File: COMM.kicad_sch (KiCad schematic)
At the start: 14 parts, among them J1 SMA Conn. (RFPC-SMA30-F), SW1 Inhibit Switch (SS5GLD2), U1 XBee Module (XBP9B-DMSTB002)

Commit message: Addressed most comments from McPherson, modified schematic.
Signed-off-by: Logan Tolbert <xem6df@virginia.edu>
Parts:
- removed D2: Voltage Converter DMR (1N4002), Diode_THT:D_DO-41_SOD81_P10.16mm_Horizontal, symbol Diode:1N4002
- added C2: 10 μF, C_10uF:CAPC1005X70N, symbol Device:C
- added D1: GRN_DMR, LED_THT:LED_D5.0mm, symbol Device:LED
- added R3: 140 Ω, R_470O:RESC6332X65N, symbol Device:R_US
- D2: renamed from D1; value LED -> GRN_XB
- D3: value LED -> YLW_ASC_XB
- R1: value 10 kΩ -> 130 Ω; footprint R_10kO:RESC1005X40N -> R_470O:RESC6332X65N
- R2: value 470 Ω -> 130 Ω
- renumbered C2 to C3, C3 to C4, C4 to C5
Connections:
- net +3.3V: now also R2.2
- net Associate/DIO5_XB: now also R3.2; no longer D3.2 (A)
- net GND: now also C2.2, D1.1 (K); no longer R1.1
- net Voltage Converter/VIN: no longer R2.2
- net at SW1.3 (C): no longer R1.2
- net Voltage Step-Up (TPS61085)/VIN: now reaches H1.51
- net Voltage Step-Up (TPS61085)/VIN: now also R1.2, C2.1
- net HST_RXD_DMR: no longer names the net of H2.25
- net HST_TXD_DMR: no longer names the net of H2.27
- new net: D1.2 (A), R1.1
- new net: D3.2 (A), R3.1
- no-connect marks 24 -> 27
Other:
- sheet DMR818S-U 2W RF Module renamed DMR818S 5W RF Module
- sheet Voltage Converter XB renamed Voltage Converter
- added sheet Voltage Step-Up (TPS61085) (TPS61085.kicad_sch)
- sheet DMR818S 5W RF Module ports: added none; removed HST_RXD, HST_TXD
- note added: "5V Power Supply From EPS for XBee Module"
- note added: "D3-LED ON indicates XBee is enabled."
- note removed: "5V Power Supply From EPS"
- moved on the sheet: C1, C3, C4, C5, D2, D3, H1, H2, J1, R2, SW1, U1

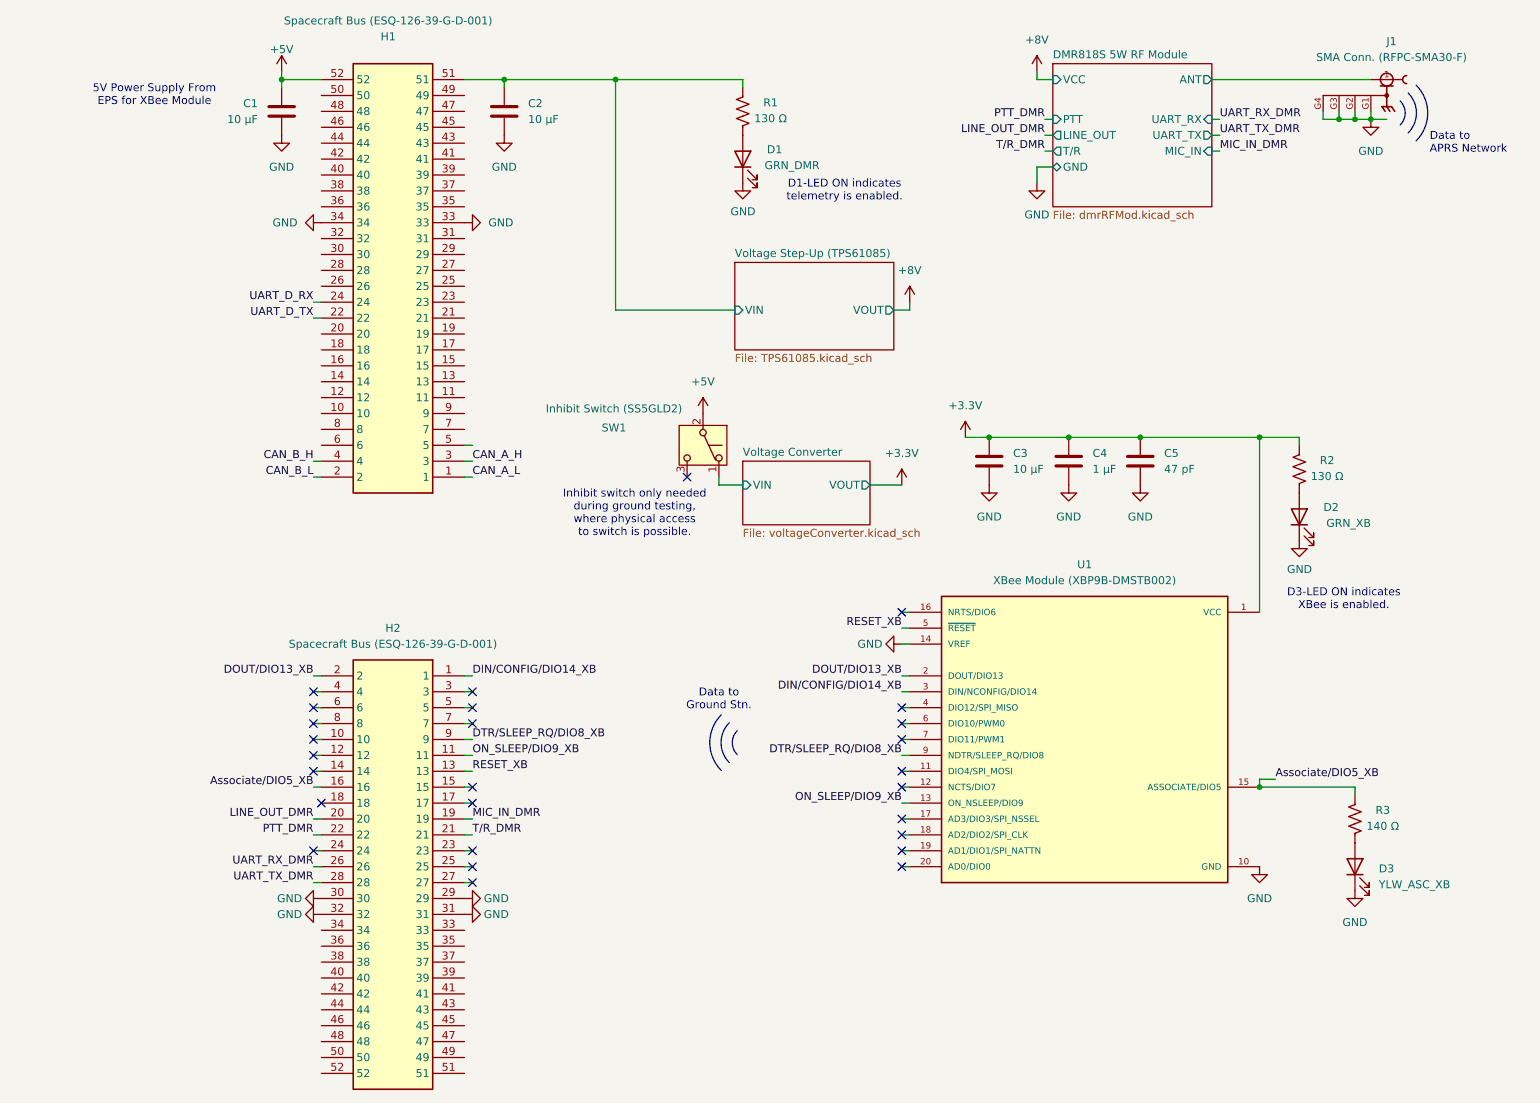
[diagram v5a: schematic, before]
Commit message: Finalized board design, updated DMR module to DMR818S-5W exact dimensions, rerouted PCB according to McPherson's comments. Added TLV61047 5V to 8V booster module.
Signed-off-by: Logan Tolbert <xem6df@virginia.edu>
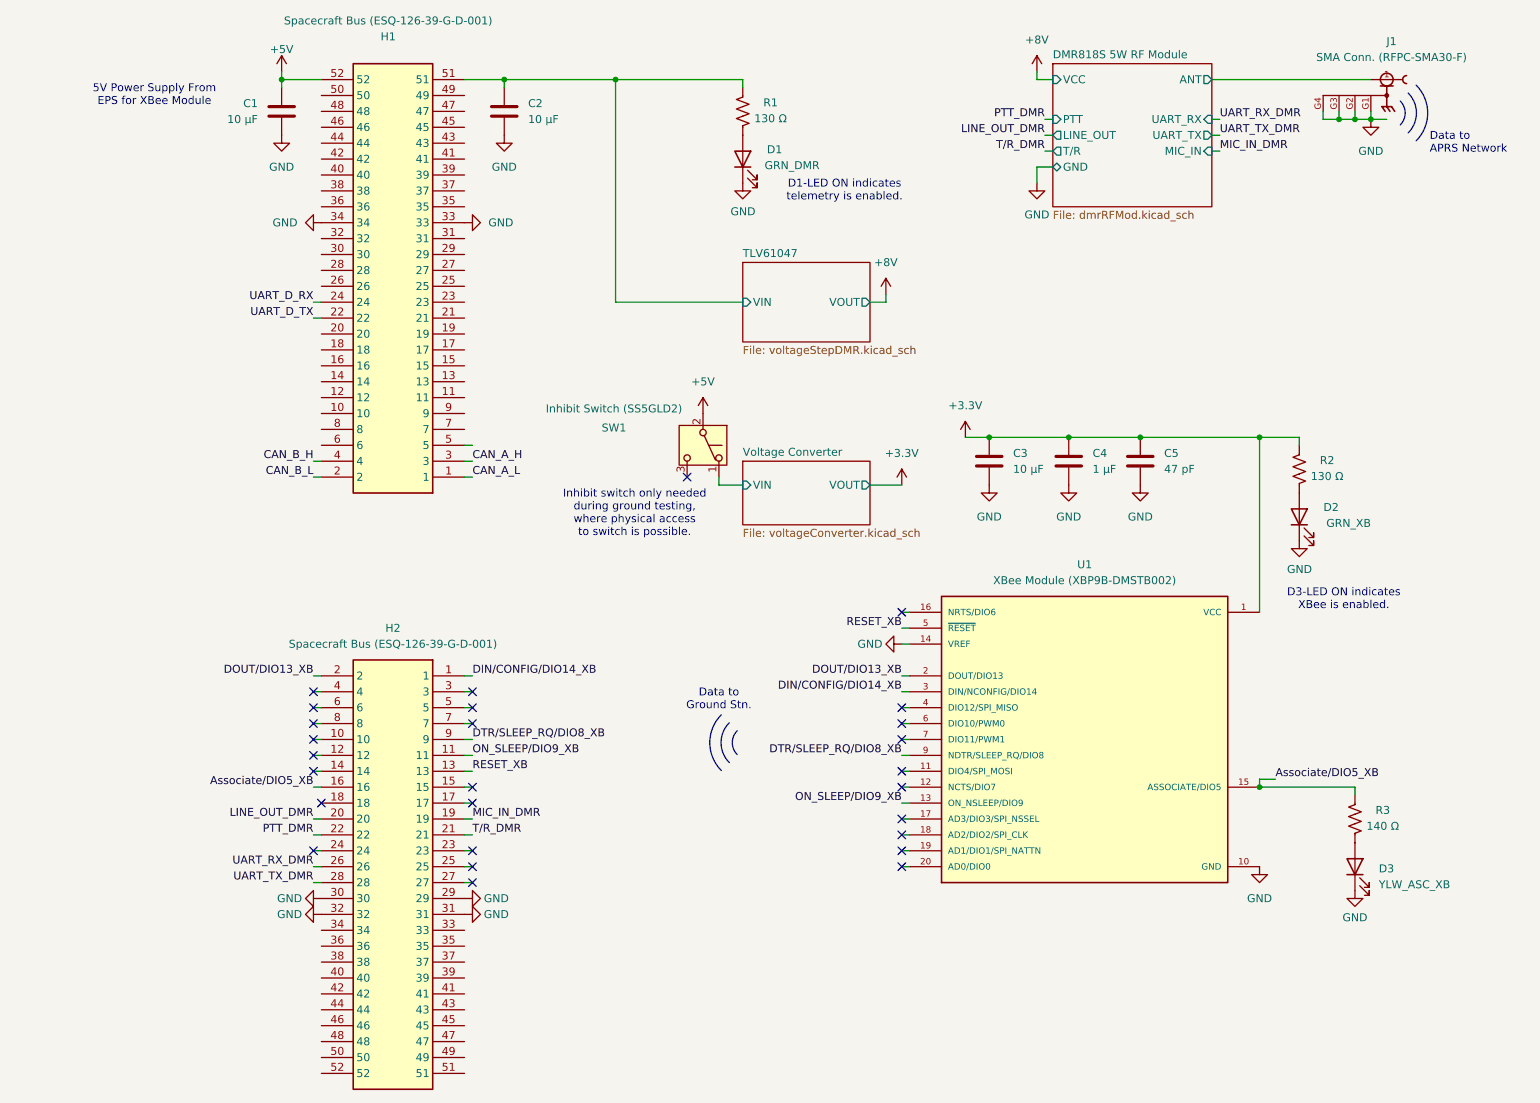
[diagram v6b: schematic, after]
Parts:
- D1, D2: footprint LED_THT:LED_D5.0mm -> LED_THT:LED_D3.0mm
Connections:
- net Voltage Step-Up (TPS61085)/VIN renamed TLV61047/VIN
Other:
- removed sheet Voltage Step-Up (TPS61085)
- added sheet TLV61047 (voltageStepDMR.kicad_sch)
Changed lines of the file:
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@@
 	(wire
 		(pts
-			(xy 170.18 67.31) (xy 167.64 67.31)
+			(xy 166.37 66.04) (xy 163.83 66.04)
 		)
 		(stroke
@@
 	(wire
 		(pts
-			(xy 123.19 67.31) (xy 142.24 67.31)
+			(xy 123.19 66.04) (xy 143.51 66.04)
 		)
 		(stroke
@@
 	(wire
 		(pts
-			(xy 170.18 66.04) (xy 170.18 67.31)
+			(xy 166.37 64.77) (xy 166.37 66.04)
 		)
 		(stroke
@@
 	(wire
 		(pts
-			(xy 123.19 30.48) (xy 123.19 67.31)
+			(xy 123.19 30.48) (xy 123.19 66.04)
 		)
 		(stroke
@@
 	(symbol
 		(lib_id "power:+8V")
-		(at 170.18 66.04 0)
+		(at 166.37 64.77 0)
 		(unit 1)
 		(exclude_from_sim no)
@@
 		(dnp no)
 		(fields_autoplaced yes)
-		(property "Reference" "#PWR014"
-			(at 170.18 69.85 0)
+		(property "Reference" "#PWR012"
+			(at 166.37 68.58 0)
 			(effects
 				(font
@@
 		)
 		(property "Value" "+8V"
-			(at 170.18 60.96 0)
+			(at 166.37 59.69 0)
 			(effects
 				(font
@@
 		)
 		(property "Footprint" ""
-			(at 170.18 66.04 0)
+			(at 166.37 64.77 0)
 			(effects
 				(font
@@
 		)
 		(property "Datasheet" ""
-			(at 170.18 66.04 0)
+			(at 166.37 64.77 0)
 			(effects
 				(font
@@
 		)
 		(property "Description" "Power symbol creates a global label with name \"+8V\""
-			(at 170.18 66.04 0)
+			(at 166.37 64.77 0)
 			(effects
 				(font
@@
 			(project ""
 				(path "/b0bd204d-ca77-4624-acd2-31813bf00a6c"
-					(reference "#PWR014")
+					(reference "#PWR012")
 					(unit 1)
 				)
@@
 			)
 		)
-		(property "Footprint" "LED_THT:LED_D5.0mm"
+		(property "Footprint" "LED_THT:LED_D3.0mm"
 			(at 232.41 100.33 0)
 			(effects
@@
 		(on_board yes)
 		(dnp no)
-		(property "Reference" "#PWR013"
+		(property "Reference" "#PWR014"
 			(at 162.56 120.65 0)
 			(effects
@@
 			(project ""
 				(path "/b0bd204d-ca77-4624-acd2-31813bf00a6c"
-					(reference "#PWR013")
+					(reference "#PWR014")
 					(unit 1)
 				)
@@
 			)
 		)
-		(property "Footprint" "LED_THT:LED_D5.0mm"
+		(property "Footprint" "LED_THT:LED_D3.0mm"
 			(at 143.51 43.18 0)
 			(effects
@@
 		(dnp no)
 		(fields_autoplaced yes)
-		(property "Reference" "#PWR012"
+		(property "Reference" "#PWR013"
 			(at 168.91 99.06 0)
 			(effects
@@
 			(project ""
 				(path "/b0bd204d-ca77-4624-acd2-31813bf00a6c"
-					(reference "#PWR012")
+					(reference "#PWR013")
 					(unit 1)
 				)
@@
 		(on_board yes)
 		(dnp no)
-		(fields_autoplaced yes)
 		(property "Reference" "#PWR023"
 			(at 241.3 166.37 0)
@@
 		)
 		(property "Value" "GND"
-			(at 241.3 165.1 0)
+			(at 241.3 164.338 0)
 			(effects
 				(font
@@
 	)
 	(sheet
-		(at 142.24 59.69)
-		(size 25.4 13.97)
+		(at 143.51 59.69)
+		(size 20.32 12.7)
 		(exclude_from_sim no)
 		(in_bom yes)
@@
 			(color 0 0 0 0.0000)
 		)
-		(property "Sheetname" "Voltage Step-Up (TPS61085)"
-			(at 142.24 58.9784 0)
+		(property "Sheetname" "TLV61047"
+			(at 143.51 58.9784 0)
 			(effects
 				(font
@@
 			)
 		)
-		(property "Sheetfile" "TPS61085.kicad_sch"
-			(at 142.24 74.2446 0)
+		(property "Sheetfile" "voltageStepDMR.kicad_sch"
+			(at 143.51 72.9746 0)
 			(effects
 				(font
@@
 		)
 		(pin "VIN" input
-			(at 142.24 67.31 180)
+			(at 143.51 66.04 180)
 			(effects
 				(font
@@
 		)
 		(pin "VOUT" output
-			(at 167.64 67.31 0)
+			(at 163.83 66.04 0)
 			(effects
 				(font

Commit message: Final COMM board design as of Feb 12 2026, ready to order.
Signed-off-by: Logan Tolbert <xem6df@virginia.edu>
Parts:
- removed SW1: Inhibit Switch (SS5GLD2), Inhibit_Switch_COMM:SS5GLD2, symbol Switch:SW_Push_SPDT
- added S1: SS-5GLD2, Inhibit_Switch_COMM:SS5GLD2, symbol SS-5GLD2:SS-5GLD2
- D1: value GRN_DMR -> GRN_8V
- D3: renamed from D2; value GRN_XB -> RED_3V3
- R1: value 130 Ω -> 250 Ω; footprint R_470O:RESC6332X65N -> R_250O:RESC2012X65N
- R2: renamed from R3; footprint R_470O:RESC6332X65N -> R_140O:RESC3216X70N
- R3: renamed from R2; value 130 Ω -> 110 Ω; footprint R_470O:RESC6332X65N -> R_110O:RESC1508X55N
- renumbered D3 to D2
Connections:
- net +5V: now also S1.1 (COM)
- net +8V: now also R1.2
- net TLV61047/VIN: no longer R1.2
- net Voltage Converter/VIN: now also S1.3 (NC)
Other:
- note added: "D1-LED ON indicates 8V rail is enabled."
- note added: "D2-LED ON indicates 3.3V rail is enabled."
- note removed: "D1-LED ON indicates telemetry is enabled."
- note removed: "D3-LED ON indicates XBee is enabled."
- moved on the sheet: D1, D2, D3, R1, R2, R3

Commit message: Updated LEDs and associated resistors on board. COMM board is ready to be reordered.
Signed-off-by: Logan Tolbert <xem6df@virginia.edu>
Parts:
- D1, D2, D3: footprint LED_THT:LED_D3.0mm -> LED_THT:LED_D5.0mm
- R1: value 250 Ω -> 220 Ω; footprint R_250O:RESC2012X65N -> Resistor_SMD:R_0603_1608Metric
- R2: value 140 Ω -> 62 Ω; footprint R_140O:RESC3216X70N -> Resistor_SMD:R_0603_1608Metric
- R3: value 110 Ω -> 62 Ω; footprint R_110O:RESC1508X55N -> Resistor_SMD:R_0603_1608Metric
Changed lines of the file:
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@@
 			)
 		)
-		(property "Value" "110 Ω"
+		(property "Value" "62 Ω"
 			(at 240.03 93.726 0)
 			(effects
@@
 			)
 		)
-		(property "Footprint" "R_110O:RESC1508X55N"
+		(property "Footprint" "Resistor_SMD:R_0603_1608Metric"
 			(at 234.696 92.456 90)
 			(effects
@@
 			)
 		)
-		(property "Footprint" "LED_THT:LED_D3.0mm"
+		(property "Footprint" "LED_THT:LED_D5.0mm"
 			(at 233.68 100.33 0)
 			(effects
@@
 			)
 		)
-		(property "Value" "250 Ω"
+		(property "Value" "220 Ω"
 			(at 180.34 60.706 0)
 			(effects
@@
 			)
 		)
-		(property "Footprint" "R_250O:RESC2012X65N"
+		(property "Footprint" "Resistor_SMD:R_0603_1608Metric"
 			(at 175.006 59.436 90)
 			(effects
@@
 			)
 		)
-		(property "Footprint" "LED_THT:LED_D3.0mm"
+		(property "Footprint" "LED_THT:LED_D5.0mm"
 			(at 173.99 67.31 0)
 			(effects
@@
 			)
 		)
-		(property "Value" "140 Ω"
+		(property "Value" "62 Ω"
 			(at 238.506 149.606 0)
 			(effects
@@
 			)
 		)
-		(property "Footprint" "R_140O:RESC3216X70N"
+		(property "Footprint" "Resistor_SMD:R_0603_1608Metric"
 			(at 233.426 148.336 90)
 			(effects
@@
 			)
 		)
-		(property "Footprint" "LED_THT:LED_D3.0mm"
+		(property "Footprint" "LED_THT:LED_D5.0mm"
 			(at 232.41 156.21 0)
 			(effects
